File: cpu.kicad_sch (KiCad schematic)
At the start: 29 parts, among them J1 USB_C_Receptacle, SW1 TL3342F160QG/TR, SW2 TL3342F160QG/TR, U4 RP2040, U5 LM4040DBZ-3, U6 W25Q32JVSS, Y1 Crystal

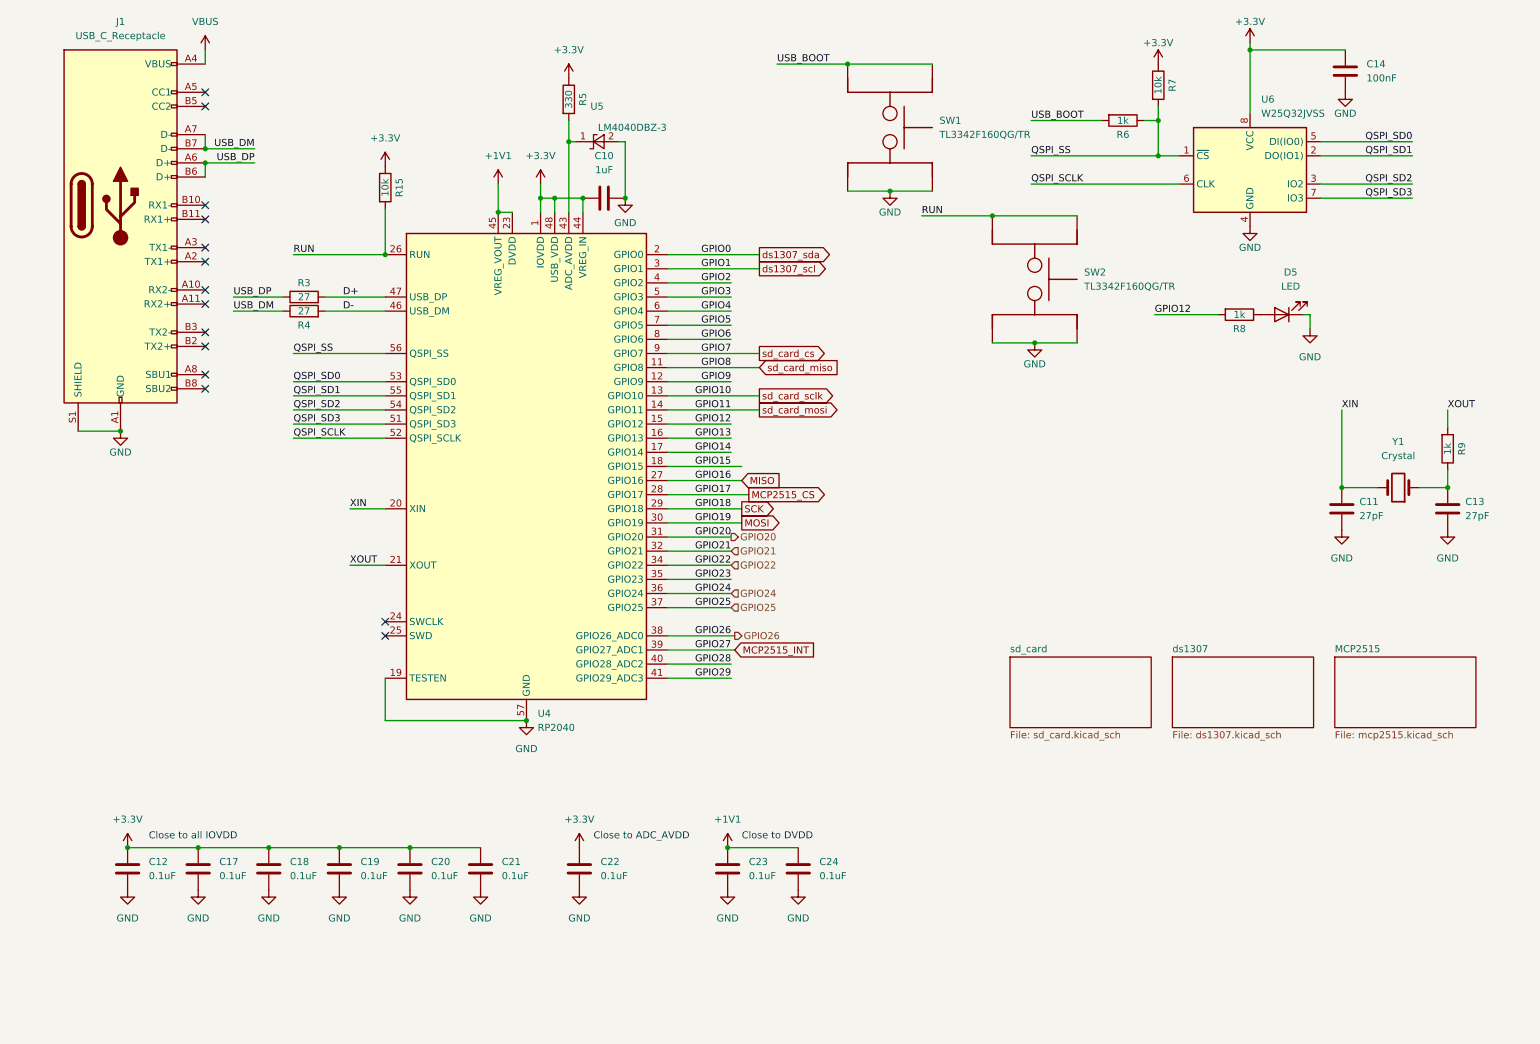
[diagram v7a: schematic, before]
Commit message: Added schematic descriptions
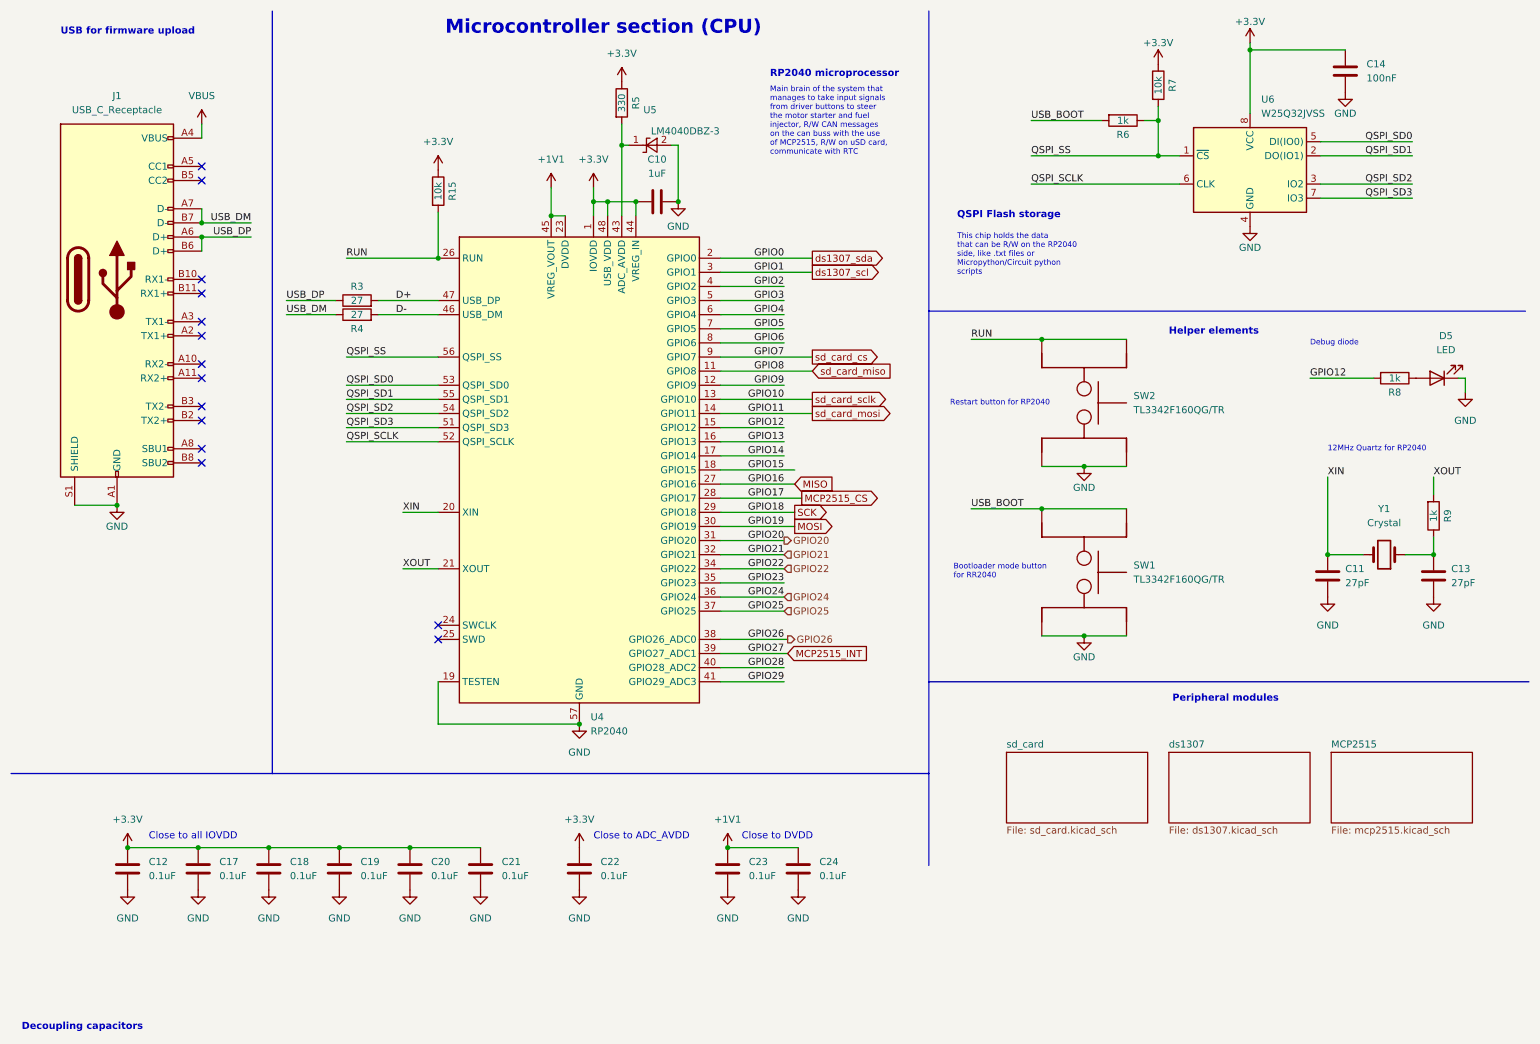
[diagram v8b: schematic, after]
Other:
- note added: "12MHz Quartz for RP2040"
- note added: "Bootloader mode button for RR2040"
- note added: "Debug diode"
- note added: "Decoupling capacitors"
- note added: "Helper elements"
- note added: "Main brain of the system that manages to take input signals from driver buttons to steer the motor starter and fuel injector, R/W CAN messages on the can buss with the use of MCP2515, R/W on uSD card, communicate with RTC"
- note added: "Microcontroller section (CPU)"
- note added: "Peripheral modules"
- note added: "QSPI Flash storage"
- note added: "RP2040 microprocessor"
- note added: "Restart button for RP2040"
- note added: "This chip holds the data that can be R/W on the RP2040 side, like .txt files or Micropython/Circuit python scripts"
- note added: "USB for firmware upload"
- moved on the sheet: C10, C11, C13, D5, J1, R15, R3, R4, R5, R8, R9, SW1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
